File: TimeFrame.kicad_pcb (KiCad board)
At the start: 2 copper layers, 100 x 100 mm, 7 parts, among them J1 USB4105-GF-A

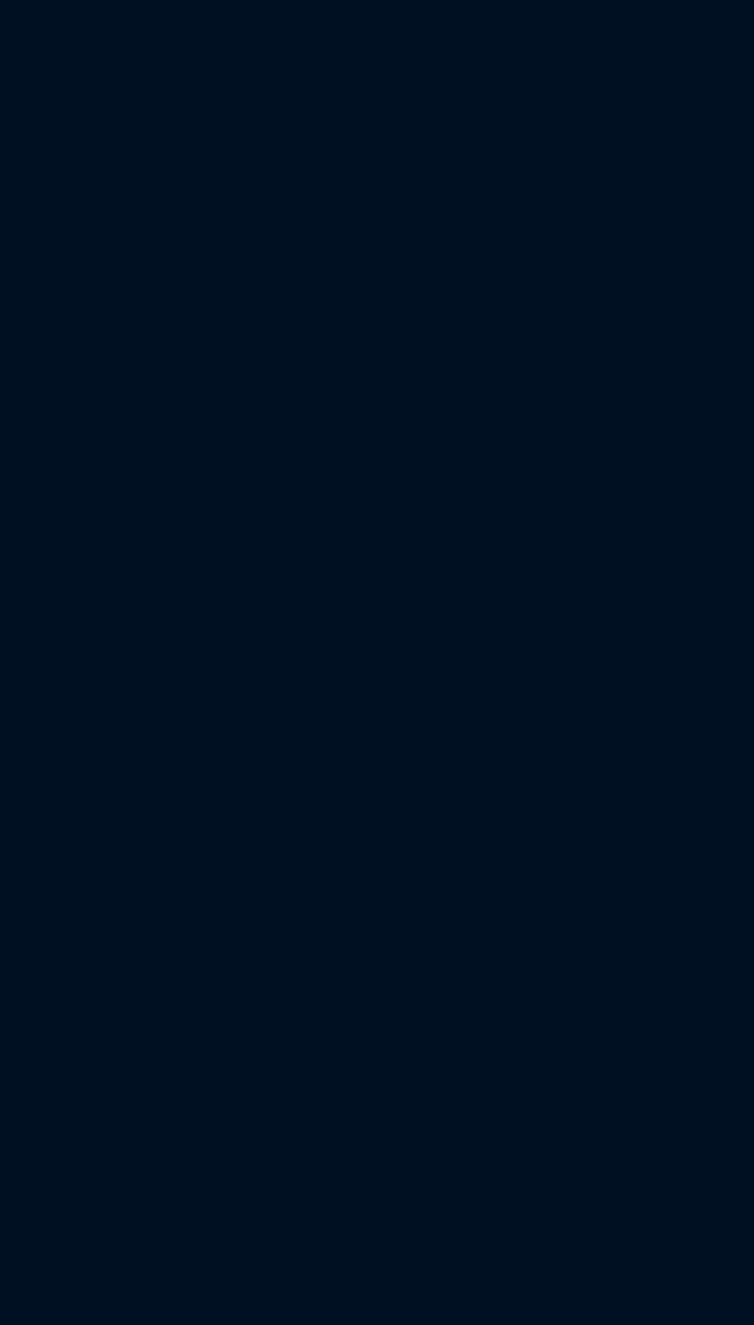
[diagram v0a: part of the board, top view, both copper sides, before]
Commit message: Adding Encoders
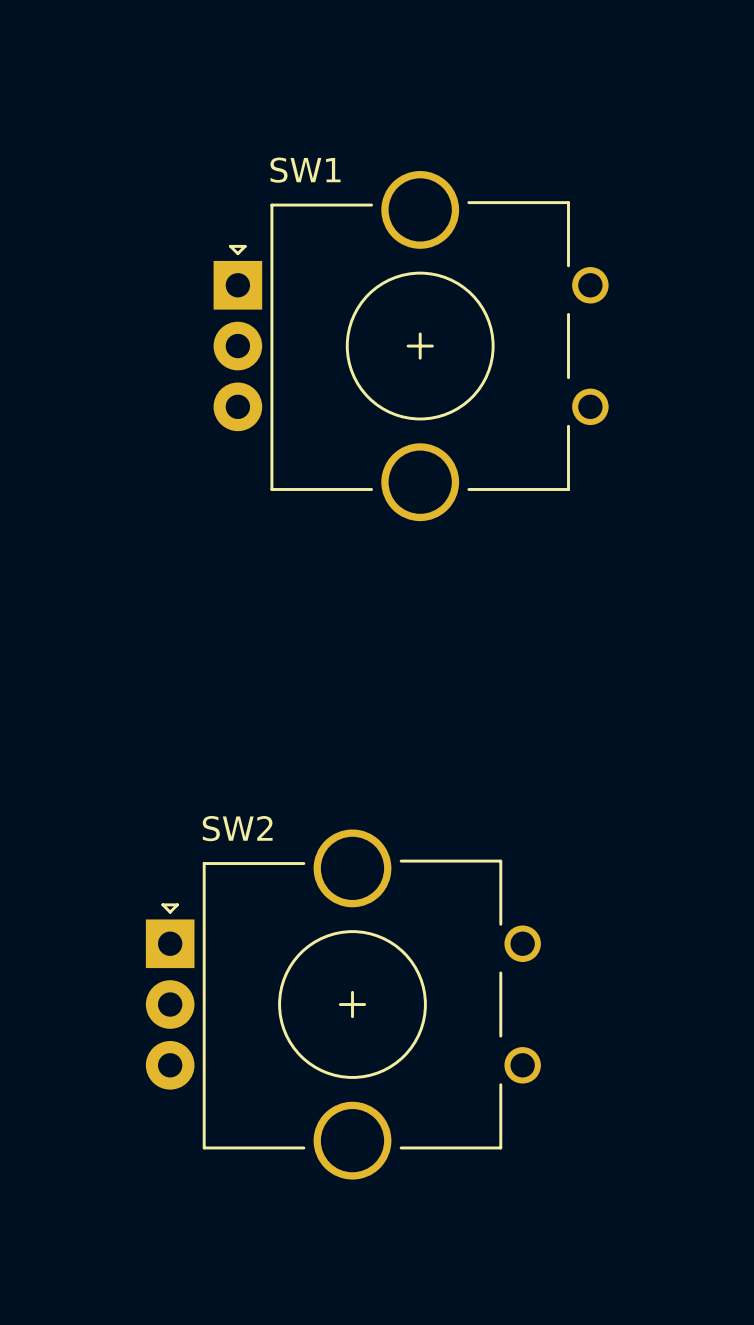
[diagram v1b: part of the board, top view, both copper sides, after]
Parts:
- added SW1: RotaryEncoder_Switch_MP, AC-kicad-library:RotaryEncoder_Bourns_PEC11R-4220F-S0024_Vertical_H20mm_CircularMountingHoles, F.Cu at (101.3, 69.2)
- added SW2: RotaryEncoder_Switch_MP, AC-kicad-library:RotaryEncoder_Bourns_PEC11R-4220F-S0024_Vertical_H20mm_CircularMountingHoles, F.Cu at (98.6, 96.2)
